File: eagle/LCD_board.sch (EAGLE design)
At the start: 5 parts

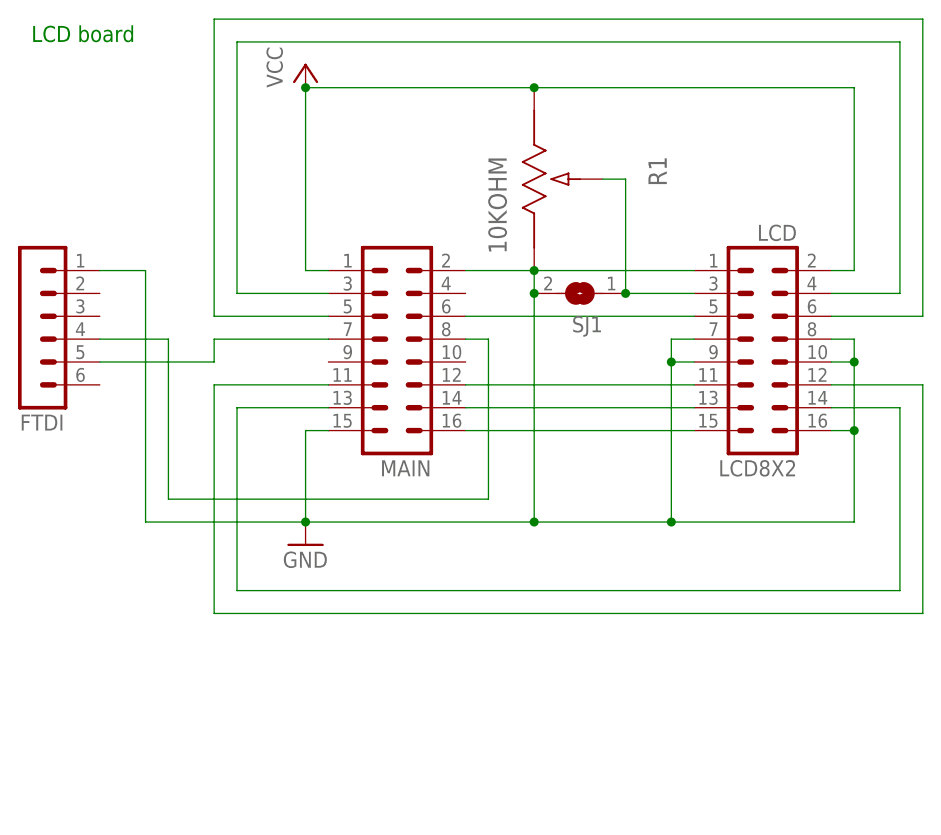
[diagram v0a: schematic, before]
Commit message: version 1.05, LCD menu added
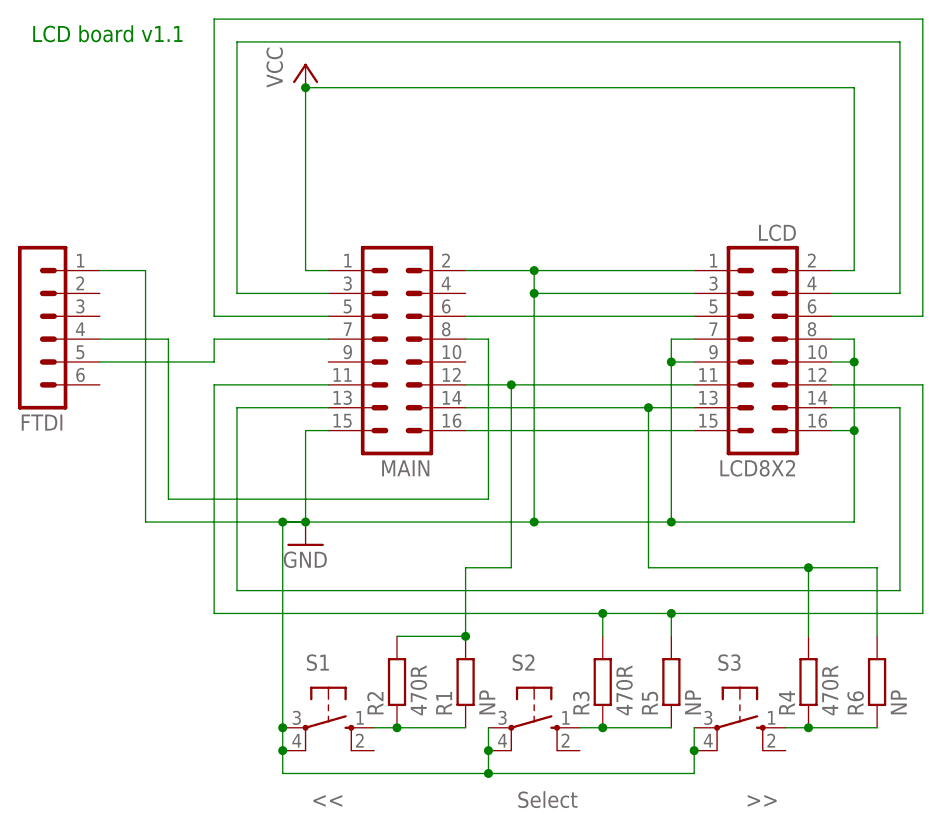
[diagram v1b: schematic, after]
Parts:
- removed SJ1: (no value), jumper:SJ
- added R2, R3, R4: 470R, resistor:R-EU_R0805
- added R5, R6: NP, resistor:R-EU_0204/7
- added S1: <<, switch-omron:10-XX
- added S2: Select, switch-omron:10-XX
- added S3: >>, switch-omron:10-XX
- R1: value 10KOHM -> NP; device Panasonic-Trimmer_Potentiometers:EVM3YSX50B14-3W -> resistor:R-EU_0204/7
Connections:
- removed net N$7: LCD8X2.3, R1.2, SJ1.1
- new net N$13: R1.1, R2.1, S1.S
- new net N$14: R3.1, R5.1, S2.S
- new net N$15: R4.1, R6.1, S3.S
- net GND: now also LCD8X2.3, S1.P, S1.P1, S2.P, S2.P1, S3.P, S3.P1; no longer R1.3, SJ1.2
- net N$3: now also R4.2, R6.2
- net N$4: now also R1.2, R2.2
- net N$8: now also R3.2, R5.2
- net VCC: no longer R1.1
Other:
- note added: "LCD board v1.1"
- note removed: "LCD board"
